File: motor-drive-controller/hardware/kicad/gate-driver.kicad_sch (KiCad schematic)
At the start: 15 parts, among them U3 DRV8305NPHP

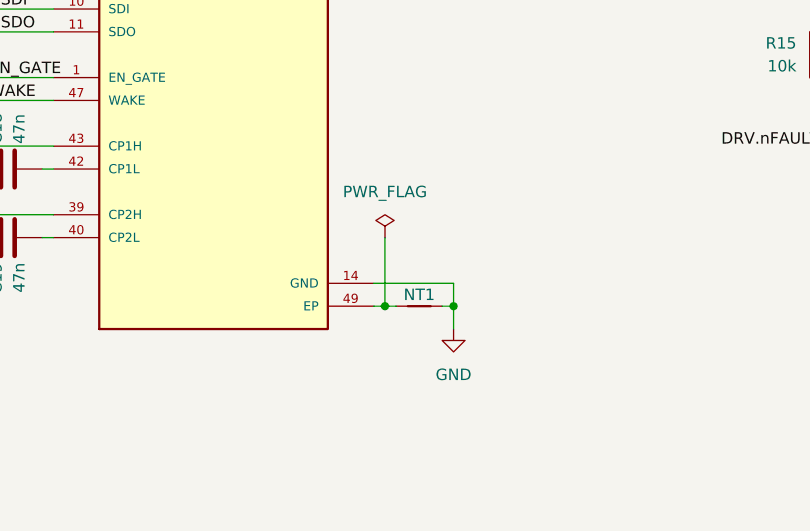
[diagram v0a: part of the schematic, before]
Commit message: fix(hw09): update ERC status and resolve multiple warnings in design notes and schematics
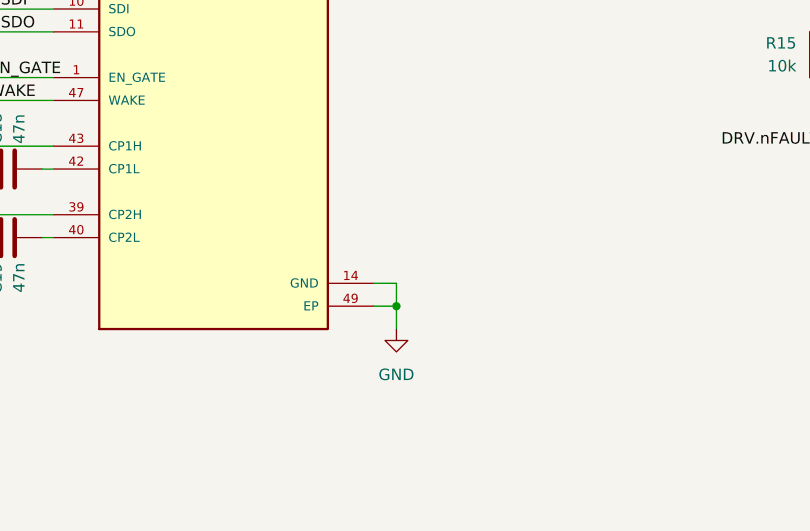
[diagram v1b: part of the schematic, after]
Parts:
- removed NT1: NetTie_2, NetTie:NetTie-2_SMD_Pad0.5mm, symbol Device:NetTie_2
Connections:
- net GND is gone; now on net EP: C16.2, C17.2, C20.2, C23.2, C24.2, C34.2, U3.14 (GND), U3.45 (GND)
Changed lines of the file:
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@@
 	)
 	(junction
-		(at 265.43 45.72)
+		(at 146.05 165.1)
 		(diameter 0)
 		(color 0 0 0 0)
 	)
 	(junction
-		(at 247.65 132.08)
+		(at 265.43 45.72)
 		(diameter 0)
 		(color 0 0 0 0)
 	)
 	(junction
-		(at 144.78 165.1)
+		(at 247.65 132.08)
 		(diameter 0)
 		(color 0 0 0 0)
@@
 	)
 	(junction
-		(at 152.4 165.1)
-		(diameter 0)
-		(color 0 0 0 0)
-	)
-	(junction
 		(at 196.85 130.81)
 		(diameter 0)
@@
 	(wire
 		(pts
+			(xy 146.05 165.1) (xy 146.05 167.64)
+		)
+		(stroke
+			(width 0)
+			(type default)
+		)
+	)
+	(wire
+		(pts
 			(xy 97.79 134.62) (xy 107.95 134.62)
 		)
@@
 	(wire
 		(pts
-			(xy 143.51 162.56) (xy 152.4 162.56)
+			(xy 143.51 162.56) (xy 146.05 162.56)
 		)
 		(stroke
@@
 	(wire
 		(pts
-			(xy 143.51 165.1) (xy 144.78 165.1)
+			(xy 106.68 149.86) (xy 107.95 149.86)
 		)
 		(stroke
@@
 	(wire
 		(pts
-			(xy 106.68 149.86) (xy 107.95 149.86)
+			(xy 99.06 157.48) (xy 96.52 157.48)
 		)
 		(stroke
@@
 	(wire
 		(pts
-			(xy 99.06 157.48) (xy 96.52 157.48)
+			(xy 97.79 96.52) (xy 107.95 96.52)
 		)
 		(stroke
@@
 	(wire
 		(pts
-			(xy 97.79 96.52) (xy 107.95 96.52)
+			(xy 143.51 43.18) (xy 156.21 43.18)
 		)
 		(stroke
@@
 	(wire
 		(pts
-			(xy 143.51 43.18) (xy 156.21 43.18)
+			(xy 143.51 81.28) (xy 156.21 81.28)
 		)
 		(stroke
@@
 	(wire
 		(pts
-			(xy 143.51 81.28) (xy 156.21 81.28)
+			(xy 193.04 146.05) (xy 193.04 140.97)
 		)
 		(stroke
@@
 	(wire
 		(pts
-			(xy 193.04 146.05) (xy 193.04 140.97)
+			(xy 143.51 165.1) (xy 146.05 165.1)
 		)
 		(stroke
@@
 	(wire
 		(pts
-			(xy 152.4 162.56) (xy 152.4 165.1)
-		)
-		(stroke
-			(width 0)
-			(type default)
-		)
-	)
-	(wire
-		(pts
 			(xy 259.08 129.54) (xy 259.08 132.08)
 		)
@@
 	(wire
 		(pts
-			(xy 144.78 165.1) (xy 146.05 165.1)
-		)
-		(stroke
-			(width 0)
-			(type default)
-		)
-	)
-	(wire
-		(pts
 			(xy 143.51 53.34) (xy 168.91 53.34)
 		)
@@
 	(wire
 		(pts
-			(xy 152.4 165.1) (xy 152.4 167.64)
+			(xy 146.05 162.56) (xy 146.05 165.1)
 		)
 		(stroke
@@
 	(wire
 		(pts
-			(xy 144.78 157.48) (xy 144.78 165.1)
-		)
-		(stroke
-			(width 0)
-			(type default)
-		)
-	)
-	(wire
-		(pts
 			(xy 143.51 83.82) (xy 156.21 83.82)
 		)
@@
 	(wire
 		(pts
-			(xy 151.13 165.1) (xy 152.4 165.1)
-		)
-		(stroke
-			(width 0)
-			(type default)
-		)
-	)
-	(wire
-		(pts
 			(xy 97.79 129.54) (xy 107.95 129.54)
 		)
@@
 	)
 	(symbol
-		(lib_id "power:PWR_FLAG")
-		(at 144.78 157.48 0)
-		(unit 1)
-		(body_style 1)
-		(exclude_from_sim no)
-		(in_bom yes)
-		(on_board yes)
-		(in_pos_files yes)
-		(dnp no)
-		(fields_autoplaced yes)
-		(property "Reference" "#FLG013"
-			(at 144.78 155.575 0)
-			(hide yes)
-			(show_name no)
-			(do_not_autoplace no)
-			(effects
-				(font
-					(size 1.27 1.27)
-				)
-			)
-		)
-		(property "Value" "PWR_FLAG"
-			(at 144.78 152.4 0)
-			(show_name no)
-			(do_not_autoplace no)
-			(effects
-				(font
-					(size 1.27 1.27)
-				)
-			)
-		)
-		(property "Footprint" ""
-			(at 144.78 157.48 0)
-			(hide yes)
-			(show_name no)
-			(do_not_autoplace no)
-			(effects
-				(font
-					(size 1.27 1.27)
-				)
-			)
-		)
-		(property "Datasheet" ""
-			(at 144.78 157.48 0)
-			(hide yes)
-			(show_name no)
-			(do_not_autoplace no)
-			(effects
-				(font
-					(size 1.27 1.27)
-				)
-			)
-		)
-		(property "Description" "Special symbol for telling ERC where power comes from"
-			(at 144.78 157.48 0)
-			(hide yes)
-			(show_name no)
-			(do_not_autoplace no)
-			(effects
-				(font
-					(size 1.27 1.27)
-				)
-			)
-		)
-		(pin "1"
-		)
-		(instances
-			(project "motor-drive-controller"
-				(path "/b8e0307a-d356-4cd3-91c6-dd251b6e910b/0c161995-df7f-44eb-a617-0aa9a9de53ee"
-					(reference "#FLG013")
-					(unit 1)
-				)
-			)
-		)
-	)
-	(symbol
 		(lib_id "Device:C")
 		(at 247.65 140.97 0)
@@
 	)
 	(symbol
-		(lib_id "Device:NetTie_2")
-		(at 148.59 165.1 0)
-		(unit 1)
-		(body_style 1)
-		(exclude_from_sim no)
-		(in_bom no)
-		(on_board yes)
-		(in_pos_files yes)
-		(dnp no)
-		(property "Reference" "NT1"
-			(at 148.59 163.83 0)
-			(show_name no)
-			(do_not_autoplace no)
-			(effects
-				(font
-					(size 1.27 1.27)
-				)
-			)
-		)
-		(property "Value" "NetTie_2"
-			(at 148.59 162.56 0)
-			(hide yes)
-			(show_name no)
-			(do_not_autoplace no)
-			(effects
-				(font
-					(size 1.27 1.27)
-				)
-			)
-		)
-		(property "Footprint" "NetTie:NetTie-2_SMD_Pad0.5mm"
-			(at 148.59 165.1 0)
-			(hide yes)
-			(show_name no)
-			(do_not_autoplace no)
-			(effects
-				(font
-					(size 1.27 1.27)
-				)
-			)
-		)
-		(property "Datasheet" ""
-			(at 148.59 165.1 0)
-			(hide yes)
-			(show_name no)
-			(do_not_autoplace no)
-			(effects
-				(font
-					(size 1.27 1.27)
-				)
-			)
-		)
-		(property "Description" "Net tie, 2 pins"
-			(at 148.59 165.1 0)
-			(hide yes)
-			(show_name no)
-			(do_not_autoplace no)
-			(effects
-				(font
-					(size 1.27 1.27)
-				)
-			)
-		)
-		(pin "1"
-		)
-		(pin "2"
-		)
-		(instances
-			(project "motor-drive-controller"
-				(path "/b8e0307a-d356-4cd3-91c6-dd251b6e910b/0c161995-df7f-44eb-a617-0aa9a9de53ee"
-					(reference "NT1")
-					(unit 1)
-				)
-			)
-		)
-	)
-	(symbol
 		(lib_id "power:+3.3V")
 		(at 196.85 129.54 0)
@@
 	(symbol
 		(lib_id "power:GND")
-		(at 152.4 167.64 0)
+		(at 146.05 167.64 0)
 		(unit 1)
 		(body_style 1)
@@
 		(fields_autoplaced yes)
 		(property "Reference" "#PWR033"
-			(at 152.4 173.99 0)
+			(at 146.05 173.99 0)
 			(hide yes)
 			(show_name no)
@@
 		)
 		(property "Value" "GND"
-			(at 152.4 172.72 0)
+			(at 146.05 172.72 0)
 			(show_name no)
 			(do_not_autoplace no)
@@
 		)
 		(property "Footprint" ""
-			(at 152.4 167.64 0)
+			(at 146.05 167.64 0)
 			(hide yes)
 			(show_name no)
@@
 		)
 		(property "Datasheet" ""
-			(at 152.4 167.64 0)
+			(at 146.05 167.64 0)
 			(hide yes)
 			(show_name no)
@@
 		)
 		(property "Description" "Power symbol creates a global label with name \"GND\" , ground"
-			(at 152.4 167.64 0)
+			(at 146.05 167.64 0)
 			(hide yes)
 			(show_name no)

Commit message: feat(hw10): reset annotate schematic
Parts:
- renumbered C34 to C15, C18 to C16, C19 to C17, C23 to C18, C16 to C19, C24 to C20, C17 to C21, C20 to C22, C21 to C23, R12 to R10, R23 to R7, R15 to R8, R16 to R9

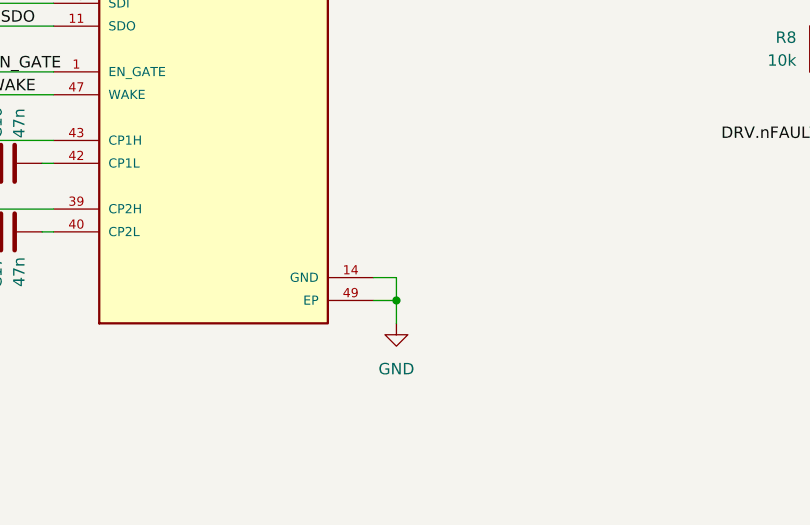
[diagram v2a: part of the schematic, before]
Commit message: feat(hw10): add NetTie_2 symbol and update related connections in gate-driver schematic
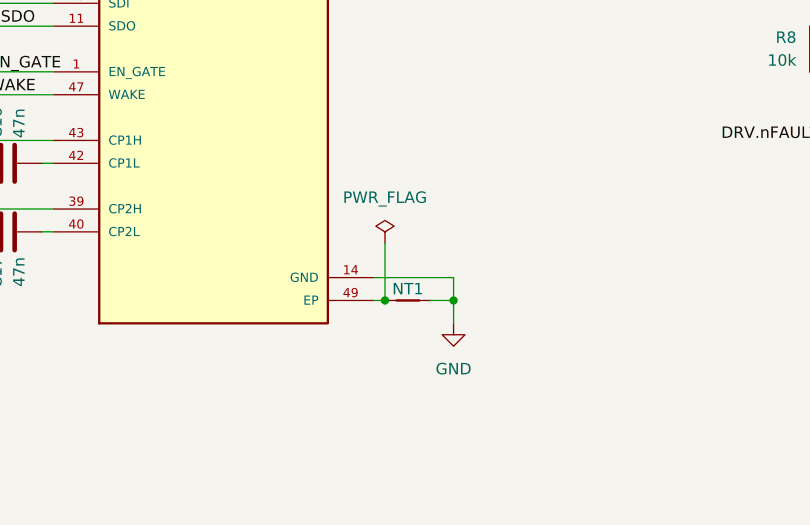
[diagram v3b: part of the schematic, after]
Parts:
- added NT1: NetTie_2, symbol Device:NetTie_2
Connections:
- net EP: now also NT1.1; no longer C15.2, C18.2, C19.2, C20.2, C21.2, C22.2, U3.14 (GND), U3.45 (GND)
- new net GND: C15.2, C18.2, C19.2, C20.2, C21.2, C22.2, NT1.2, U3.14 (GND), U3.45 (GND)
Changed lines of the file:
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@@
 	)
 	(junction
-		(at 168.91 53.34)
+		(at 144.78 165.1)
 		(diameter 0)
 		(color 0 0 0 0)
 	)
 	(junction
-		(at 255.27 45.72)
+		(at 168.91 53.34)
 		(diameter 0)
 		(color 0 0 0 0)
 	)
 	(junction
-		(at 265.43 62.23)
+		(at 255.27 45.72)
 		(diameter 0)
 		(color 0 0 0 0)
 	)
 	(junction
-		(at 146.05 165.1)
+		(at 265.43 62.23)
 		(diameter 0)
 		(color 0 0 0 0)
@@
 	)
 	(junction
+		(at 152.4 165.1)
+		(diameter 0)
+		(color 0 0 0 0)
+	)
+	(junction
 		(at 179.07 38.1)
 		(diameter 0)
@@
 	(wire
 		(pts
-			(xy 146.05 165.1) (xy 146.05 167.64)
+			(xy 152.4 162.56) (xy 152.4 165.1)
 		)
 		(stroke
@@
 	(wire
 		(pts
-			(xy 143.51 162.56) (xy 146.05 162.56)
+			(xy 143.51 162.56) (xy 152.4 162.56)
 		)
 		(stroke
@@
 	(wire
 		(pts
-			(xy 143.51 165.1) (xy 146.05 165.1)
-		)
-		(stroke
-			(width 0)
-			(type default)
-		)
-	)
-	(wire
-		(pts
 			(xy 97.79 81.28) (xy 107.95 81.28)
 		)
@@
 	(wire
 		(pts
-			(xy 179.07 38.1) (xy 179.07 40.64)
+			(xy 149.86 165.1) (xy 152.4 165.1)
 		)
 		(stroke
@@
 		)
 	)
-	(bus
+	(wire
 		(pts
-			(xy 158.75 60.96) (xy 158.75 81.28)
+			(xy 179.07 38.1) (xy 179.07 40.64)
 		)
 		(stroke
@@
 		)
 	)
-	(wire
+	(bus
 		(pts
-			(xy 274.32 41.91) (xy 274.32 45.72)
+			(xy 158.75 60.96) (xy 158.75 81.28)
 		)
 		(stroke
@@
 	(wire
 		(pts
-			(xy 200.66 130.81) (xy 200.66 133.35)
+			(xy 274.32 41.91) (xy 274.32 45.72)
 		)
 		(stroke
@@
 	(wire
 		(pts
-			(xy 97.79 73.66) (xy 107.95 73.66)
+			(xy 200.66 130.81) (xy 200.66 133.35)
 		)
 		(stroke
@@
 	(wire
 		(pts
-			(xy 97.79 58.42) (xy 107.95 58.42)
+			(xy 97.79 73.66) (xy 107.95 73.66)
 		)
 		(stroke
@@
 	(wire
 		(pts
-			(xy 146.05 162.56) (xy 146.05 165.1)
+			(xy 97.79 58.42) (xy 107.95 58.42)
 		)
 		(stroke
@@
 	(wire
 		(pts
+			(xy 143.51 165.1) (xy 144.78 165.1)
+		)
+		(stroke
+			(width 0)
+			(type default)
+		)
+	)
+	(wire
+		(pts
 			(xy 247.65 144.78) (xy 247.65 148.59)
 		)
@@
 		)
 	)
+	(wire
+		(pts
+			(xy 152.4 165.1) (xy 152.4 167.64)
+		)
+		(stroke
+			(width 0)
+			(type default)
+		)
+	)
 	(bus
 		(pts
@@
 	(wire
 		(pts
+			(xy 144.78 158.75) (xy 144.78 165.1)
+		)
+		(stroke
+			(width 0)
+			(type default)
+		)
+	)
+	(wire
+		(pts
 			(xy 96.52 149.86) (xy 96.52 147.32)
 		)
@@
 	)
 	(symbol
+		(lib_id "Device:NetTie_2")
+		(at 147.32 165.1 0)
+		(unit 1)
+		(body_style 1)
+		(exclude_from_sim no)
+		(in_bom no)
+		(on_board yes)
+		(in_pos_files yes)
+		(dnp no)
+		(property "Reference" "NT1"
+			(at 147.32 163.83 0)
+			(show_name no)
+			(do_not_autoplace no)
+			(effects
+				(font
+					(size 1.27 1.27)
+				)
+			)
+		)
+		(property "Value" "NetTie_2"
+			(at 147.32 162.56 0)
+			(hide yes)
+			(show_name no)
+			(do_not_autoplace no)
+			(effects
+				(font
+					(size 1.27 1.27)
+				)
+			)
+		)
+		(property "Footprint" ""
+			(at 147.32 165.1 0)
+			(hide yes)
+			(show_name no)
+			(do_not_autoplace no)
+			(effects
+				(font
+					(size 1.27 1.27)
+				)
+			)
+		)
+		(property "Datasheet" ""
+			(at 147.32 165.1 0)
+			(hide yes)
+			(show_name no)
+			(do_not_autoplace no)
+			(effects
+				(font
+					(size 1.27 1.27)
+				)
+			)
+		)
+		(property "Description" "Net tie, 2 pins"
+			(at 147.32 165.1 0)
+			(hide yes)
+			(show_name no)
+			(do_not_autoplace no)
+			(effects
+				(font
+					(size 1.27 1.27)
+				)
+			)
+		)
+		(pin "1"
+		)
+		(pin "2"
+		)
+		(instances
+			(project "motor-drive-controller"
+				(path "/b8e0307a-d356-4cd3-91c6-dd251b6e910b/0c161995-df7f-44eb-a617-0aa9a9de53ee"
+					(reference "NT1")
+					(unit 1)
+				)
+			)
+		)
+	)
+	(symbol
 		(lib_id "Device:R")
 		(at 200.66 137.16 0)
@@
 	)
 	(symbol
+		(lib_id "power:PWR_FLAG")
+		(at 144.78 158.75 0)
+		(unit 1)
+		(body_style 1)
+		(exclude_from_sim no)
+		(in_bom yes)
+		(on_board yes)
+		(in_pos_files yes)
+		(dnp no)
+		(fields_autoplaced yes)
+		(property "Reference" "#FLG012"
+			(at 144.78 156.845 0)
+			(hide yes)
+			(show_name no)
+			(do_not_autoplace no)
+			(effects
+				(font
+					(size 1.27 1.27)
+				)
+			)
+		)
+		(property "Value" "PWR_FLAG"
+			(at 144.78 153.67 0)
+			(show_name no)
+			(do_not_autoplace no)
+			(effects
+				(font
+					(size 1.27 1.27)
+				)
+			)
+		)
+		(property "Footprint" ""
+			(at 144.78 158.75 0)
+			(hide yes)
+			(show_name no)
+			(do_not_autoplace no)
+			(effects
+				(font
+					(size 1.27 1.27)
+				)
+			)
+		)
+		(property "Datasheet" ""
+			(at 144.78 158.75 0)
+			(hide yes)
+			(show_name no)
+			(do_not_autoplace no)
+			(effects
+				(font
+					(size 1.27 1.27)
+				)
+			)
+		)
+		(property "Description" "Special symbol for telling ERC where power comes from"
+			(at 144.78 158.75 0)
+			(hide yes)
+			(show_name no)
+			(do_not_autoplace no)
+			(effects
+				(font
+					(size 1.27 1.27)
+				)
+			)
+		)
+		(pin "1"
+		)
+		(instances
+			(project "motor-drive-controller"
+				(path "/b8e0307a-d356-4cd3-91c6-dd251b6e910b/0c161995-df7f-44eb-a617-0aa9a9de53ee"
+					(reference "#FLG012")
+					(unit 1)
+				)
+			)
+		)
+	)
+	(symbol
 		(lib_id "power:GND")
-		(at 146.05 167.64 0)
+		(at 152.4 167.64 0)
 		(unit 1)
 		(body_style 1)
@@
 		(fields_autoplaced yes)
 		(property "Reference" "#PWR031"
-			(at 146.05 173.99 0)
+			(at 152.4 173.99 0)
 			(hide yes)
 			(show_name no)
@@
 		)
 		(property "Value" "GND"
-			(at 146.05 172.72 0)
+			(at 152.4 172.72 0)
 			(show_name no)
 			(do_not_autoplace no)
@@
 		)
 		(property "Footprint" ""
-			(at 146.05 167.64 0)
+			(at 152.4 167.64 0)
 			(hide yes)
 			(show_name no)
@@
 		)
 		(property "Datasheet" ""
-			(at 146.05 167.64 0)
+			(at 152.4 167.64 0)
 			(hide yes)
 			(show_name no)
@@
 		)
 		(property "Description" "Power symbol creates a global label with name \"GND\" , ground"
-			(at 146.05 167.64 0)
+			(at 152.4 167.64 0)
 			(hide yes)
 			(show_name no)
